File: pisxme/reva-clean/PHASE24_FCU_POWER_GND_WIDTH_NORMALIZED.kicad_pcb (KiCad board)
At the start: 6 copper layers, 300 x 180 mm, 131 parts, among them J1 74221-101LF, J2 A70-112-331N126, J3 1-2199230-4, J4 Amphenol 10171746-00021LF USB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, J5 0039300020, J6 0039300020, J7 Raspberry-Pi-5-Compute-Module, Q1 CSD19536KCS, Q2 CSD19536KCS, U1 LM74700QDBVRQ1, U2 LM74700QDBVRQ1, U3 TPSM63606RDLR, U4 TPSM63606RDLR, U5 TPSM63606RDLR, U6 TPD4EUSB30, U7 TUSB9261IPVP, U8 Texas_DRT_3, U9 TPD4EUSB30, Y10 25MHz

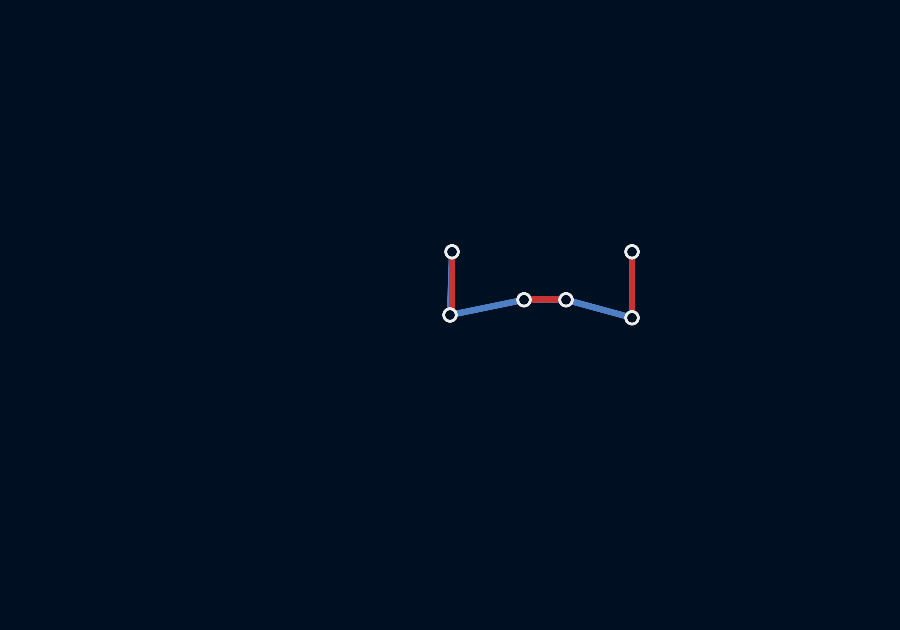
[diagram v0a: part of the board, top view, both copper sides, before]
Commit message: phase24: remove duplicate power ground via
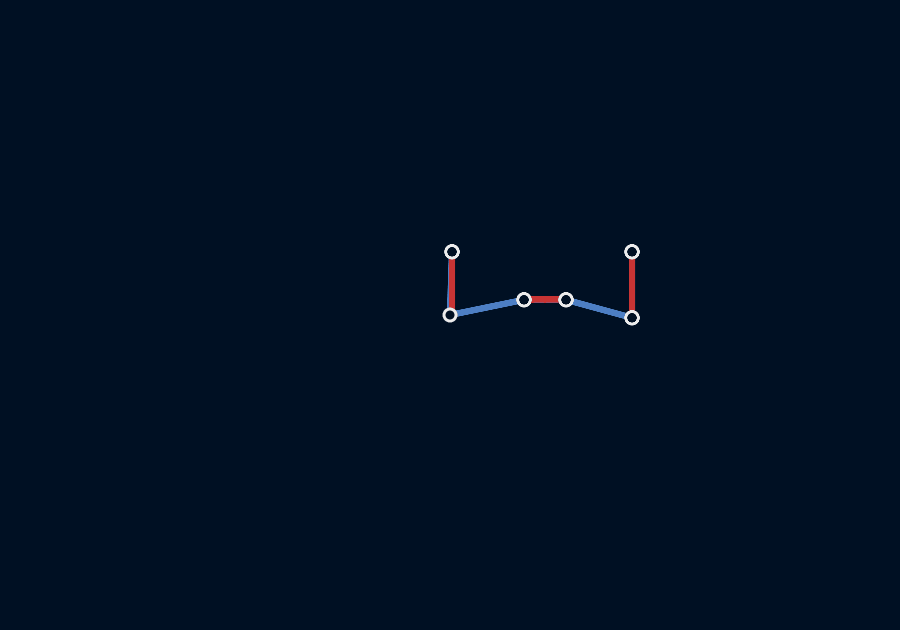
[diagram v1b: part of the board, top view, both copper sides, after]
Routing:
- net POWER_GND: vias 17 -> 16
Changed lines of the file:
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@@
-	)
-	(via
-		(at 75.032441 66.207106)
-		(size 0.5)
-		(drill 0.3)
-		(layers "F.Cu" "B.Cu")
-		(net "POWER_GND")
 	)
 	(via

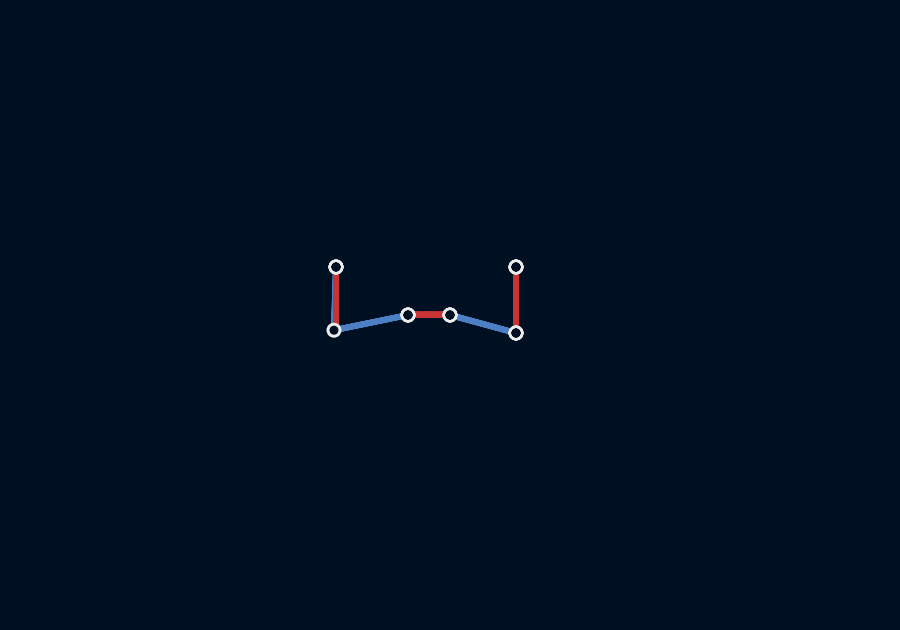
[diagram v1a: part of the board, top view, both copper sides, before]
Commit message: phase24: remove second duplicate power ground via
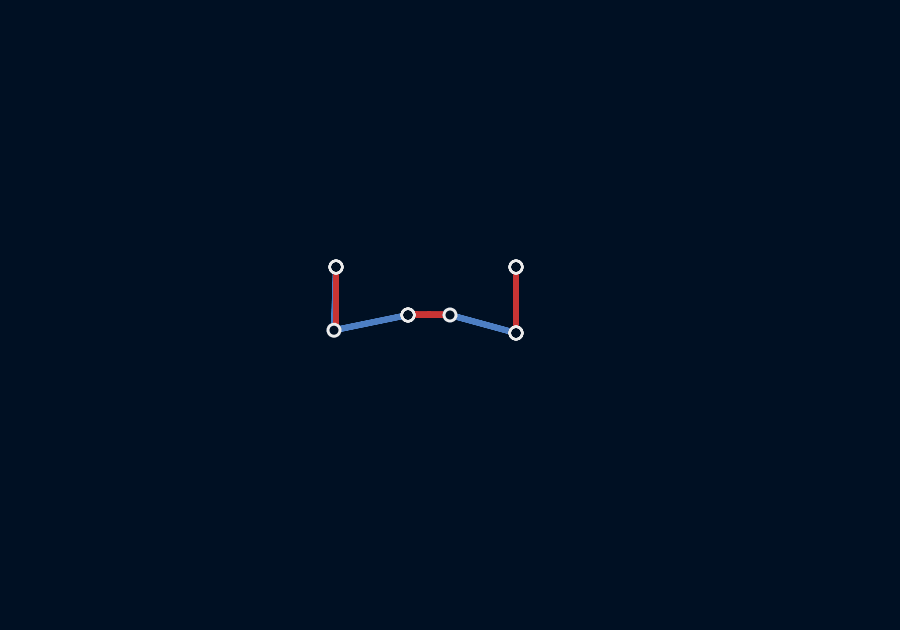
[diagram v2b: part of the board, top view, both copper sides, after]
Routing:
- net POWER_GND: vias 16 -> 15
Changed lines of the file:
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@@
-	)
-	(via
-		(at 78.9 65.699999)
-		(size 0.5)
-		(drill 0.3)
-		(layers "F.Cu" "B.Cu")
-		(net "POWER_GND")
 	)
 	(via

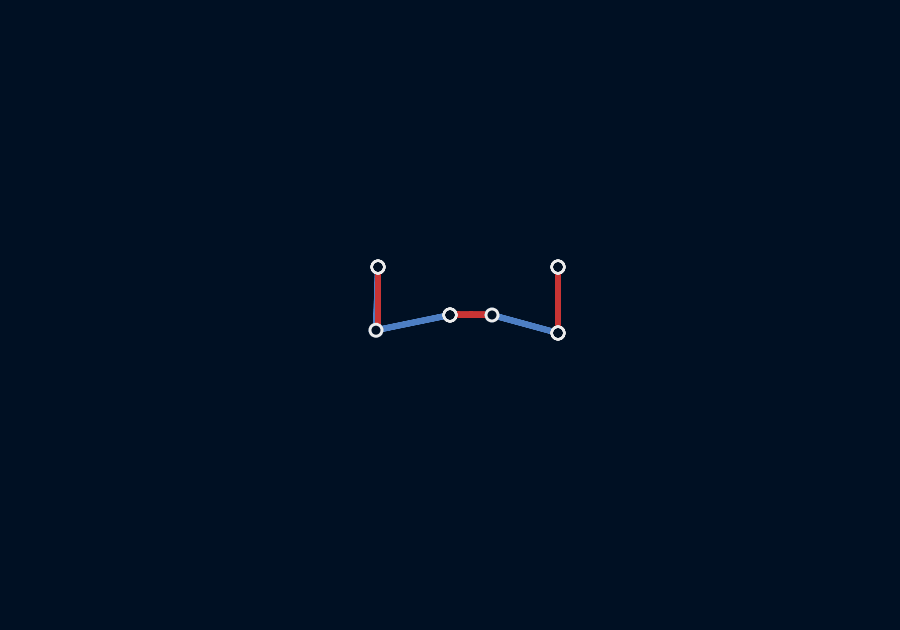
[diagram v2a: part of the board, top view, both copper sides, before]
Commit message: phase24: remove third duplicate power ground via
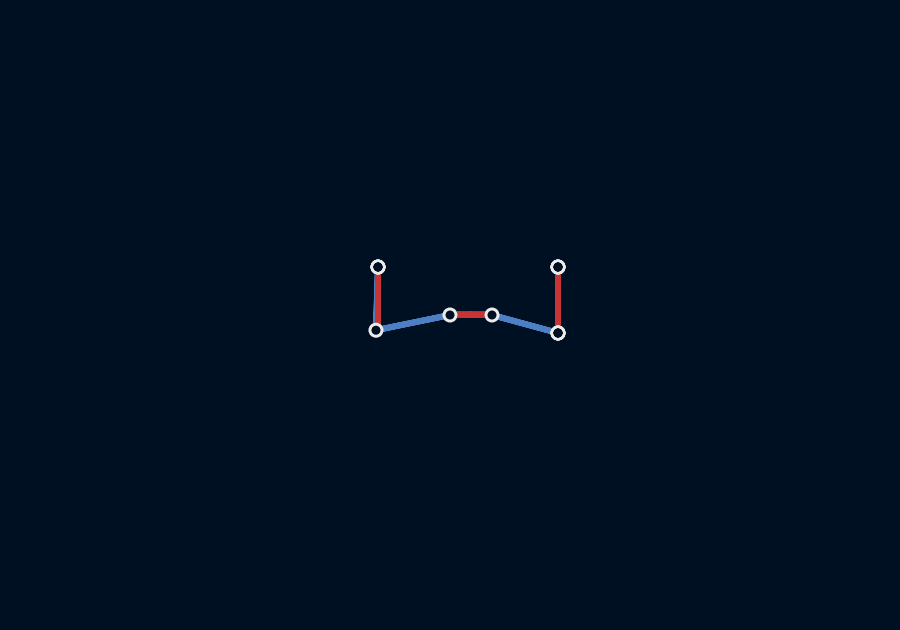
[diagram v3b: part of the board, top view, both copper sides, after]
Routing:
- net POWER_GND: vias 15 -> 14
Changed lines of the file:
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@@
-	)
-	(via
-		(at 77.5 65.699999)
-		(size 0.5)
-		(drill 0.3)
-		(layers "F.Cu" "B.Cu")
-		(net "POWER_GND")
 	)
 	(via

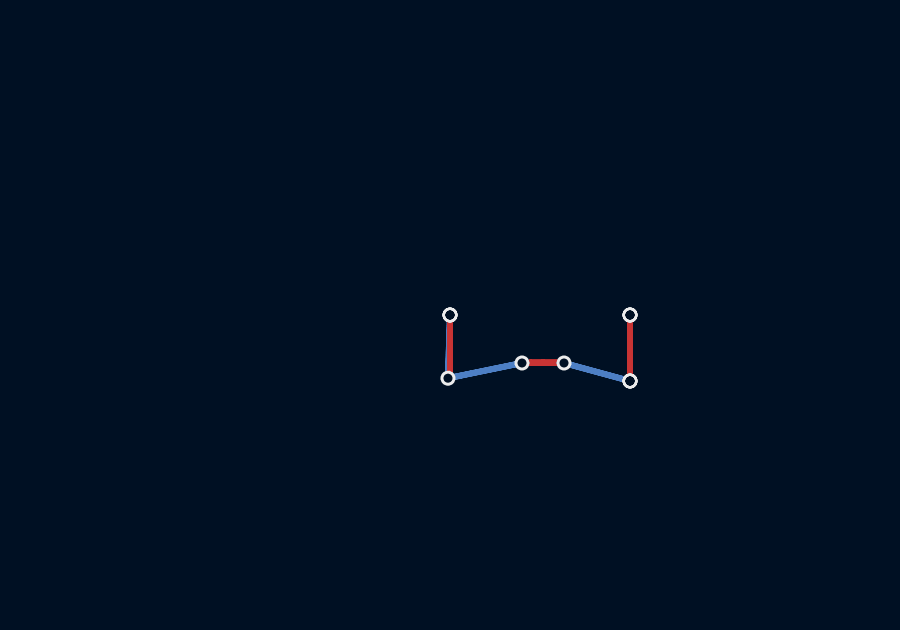
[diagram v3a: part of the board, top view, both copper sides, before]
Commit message: phase24: remove fourth duplicate power ground via
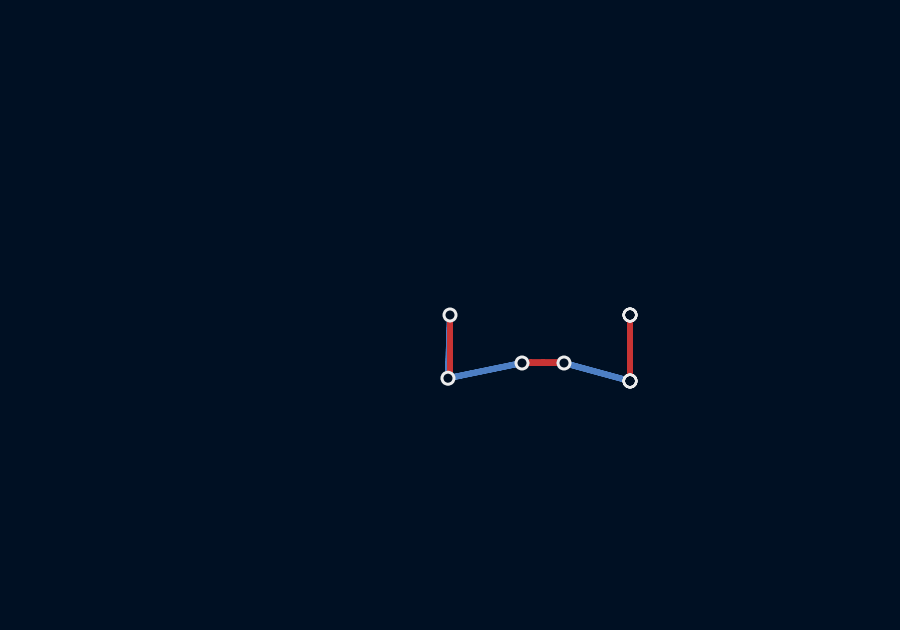
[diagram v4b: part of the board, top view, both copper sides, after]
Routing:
- net POWER_GND: vias 14 -> 13
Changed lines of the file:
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@@
-	)
-	(via
-		(at 75.1 64.099999)
-		(size 0.5)
-		(drill 0.3)
-		(layers "F.Cu" "B.Cu")
-		(net "POWER_GND")
 	)
 	(via

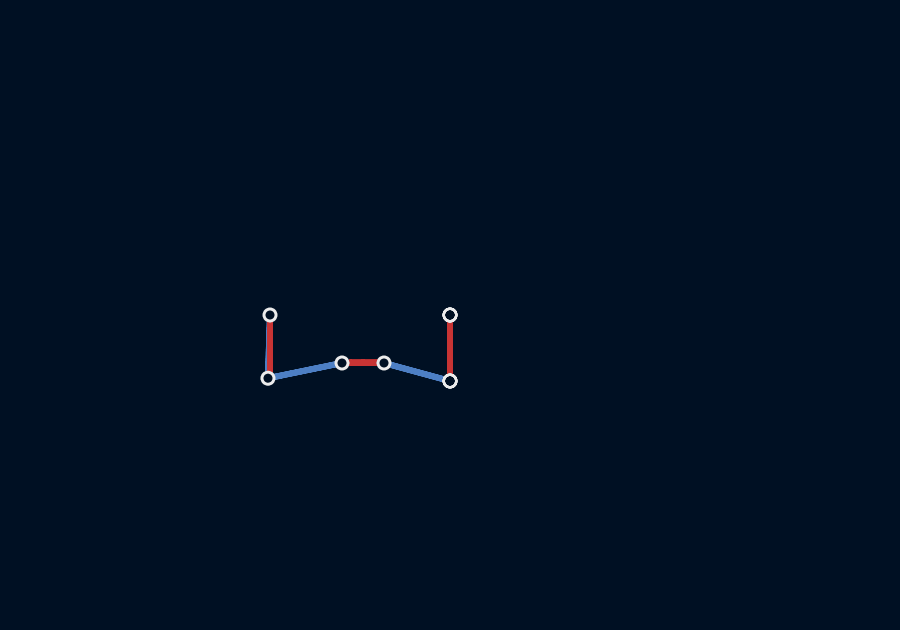
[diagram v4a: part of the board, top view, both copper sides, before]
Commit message: phase24: remove fifth duplicate power ground via
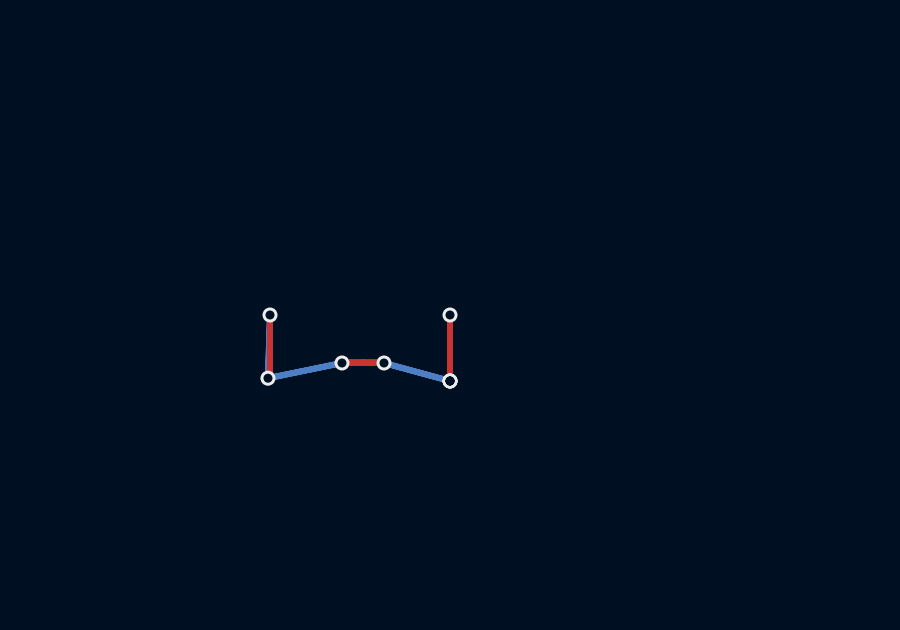
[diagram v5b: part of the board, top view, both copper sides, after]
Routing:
- net POWER_GND: vias 13 -> 12
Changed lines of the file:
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@@
-	)
-	(via
-		(at 81.1 64.099999)
-		(size 0.5)
-		(drill 0.3)
-		(layers "F.Cu" "B.Cu")
-		(net "POWER_GND")
 	)
 	(via

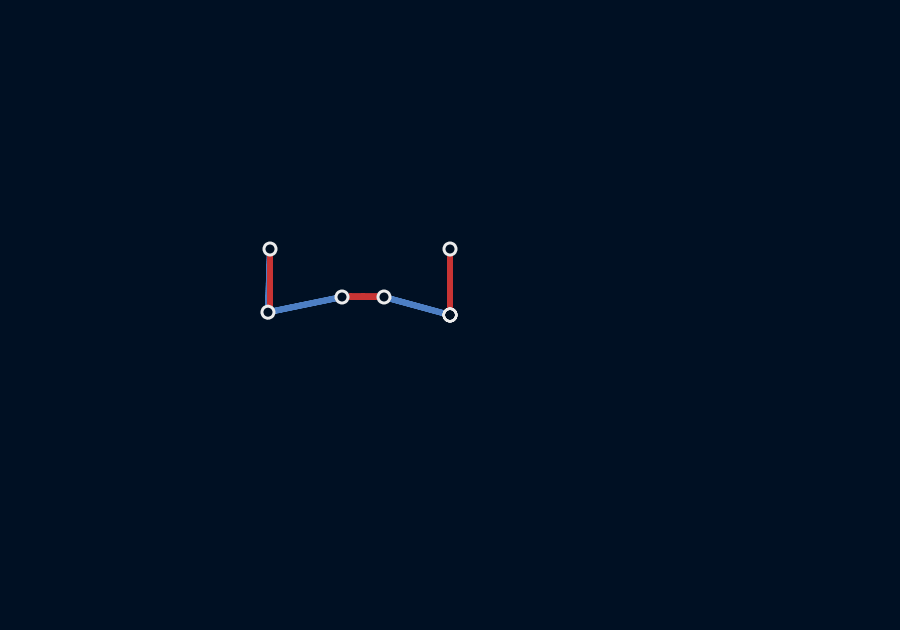
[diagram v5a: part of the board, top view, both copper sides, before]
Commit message: phase24: remove sixth duplicate power ground via
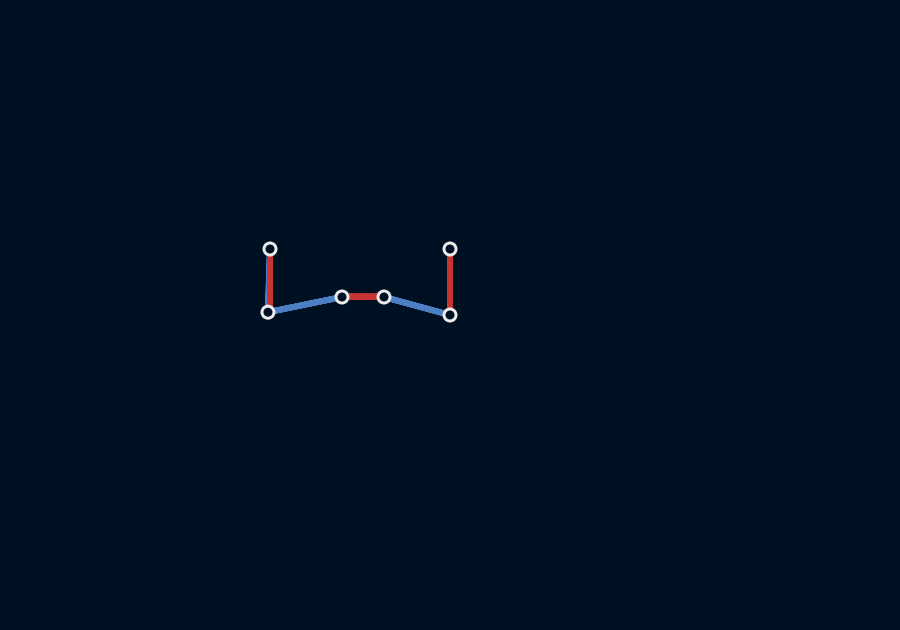
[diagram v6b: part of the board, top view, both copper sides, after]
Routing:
- net POWER_GND: vias 12 -> 11
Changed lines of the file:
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@@
-	)
-	(via
-		(at 81.1 66.3)
-		(size 0.5)
-		(drill 0.3)
-		(layers "F.Cu" "B.Cu")
-		(net "POWER_GND")
 	)
 	(via

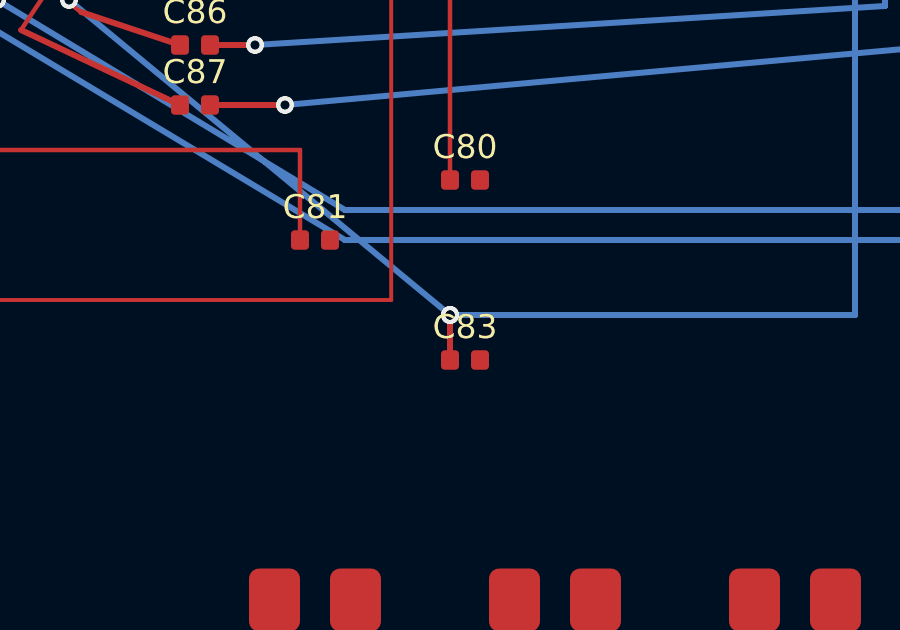
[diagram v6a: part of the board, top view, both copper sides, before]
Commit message: phase24: remove duplicate jms avddl via
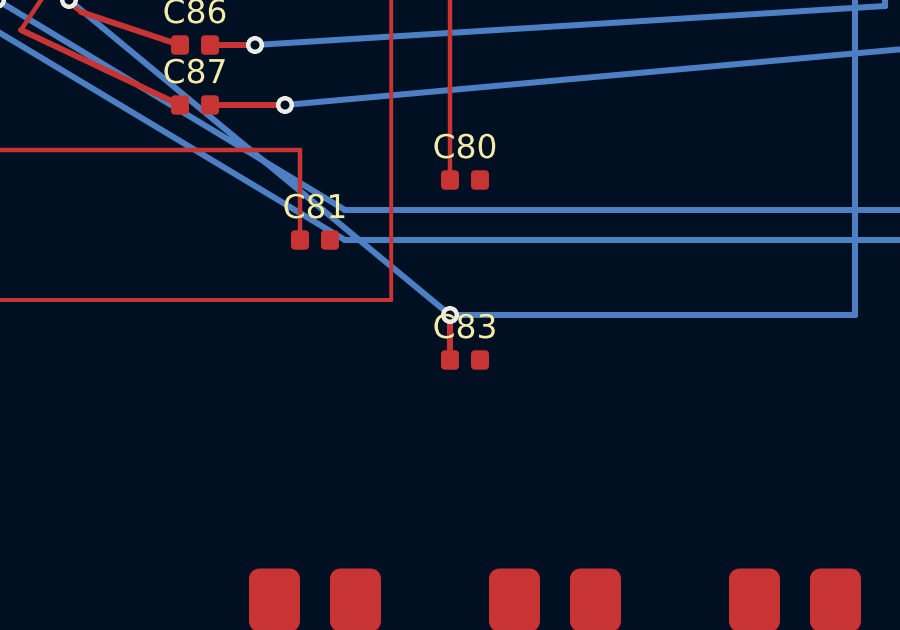
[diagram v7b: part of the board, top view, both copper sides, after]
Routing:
- net JMS_AVDDL: vias 4 -> 3
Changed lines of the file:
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@@
-	)
-	(via
-		(at 154.5 150.5)
-		(size 0.6)
-		(drill 0.3)
-		(layers "F.Cu" "B.Cu")
-		(net "JMS_AVDDL")
 	)
 	(via
